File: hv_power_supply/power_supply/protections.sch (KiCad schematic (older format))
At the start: 50 parts, among them J1 CONN_01x02, K1 CPC1979J, Q2 SSM3K333R, Q3 SSM3K333R, Q4 FQD2N60CTM, U3 CPC1117NTR, U4 ACPL-C79B-500E, U5 ACPL-C87B-000E, U6 LT-1997-2, U7 ADA4661-2

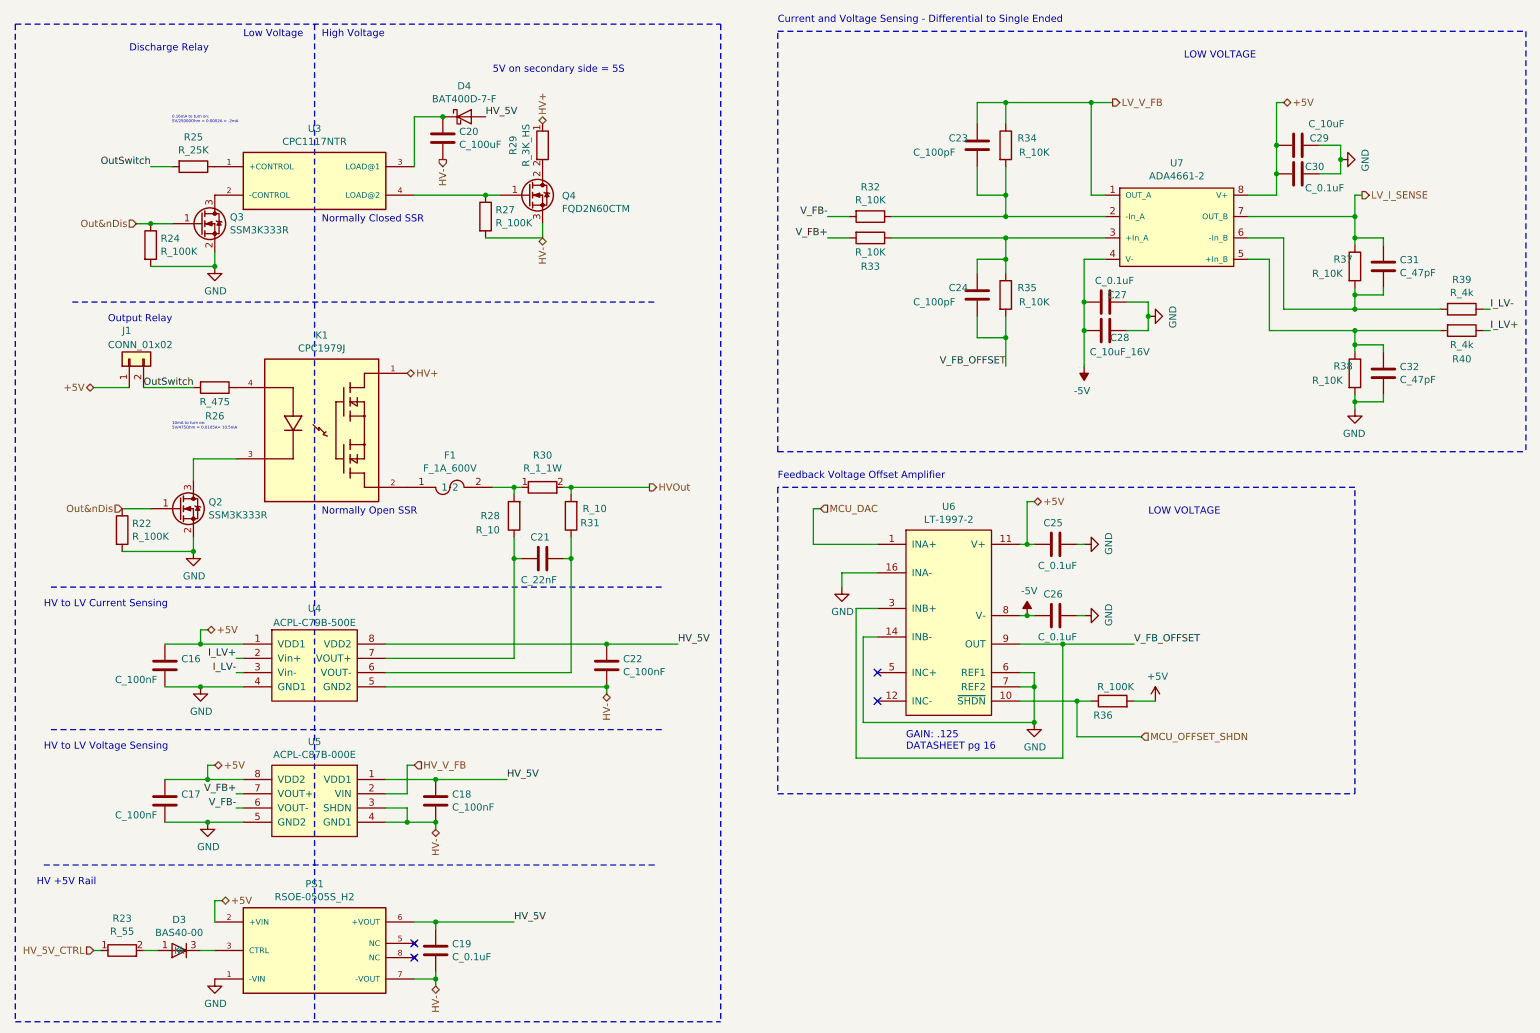
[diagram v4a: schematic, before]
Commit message: updated MCU pins
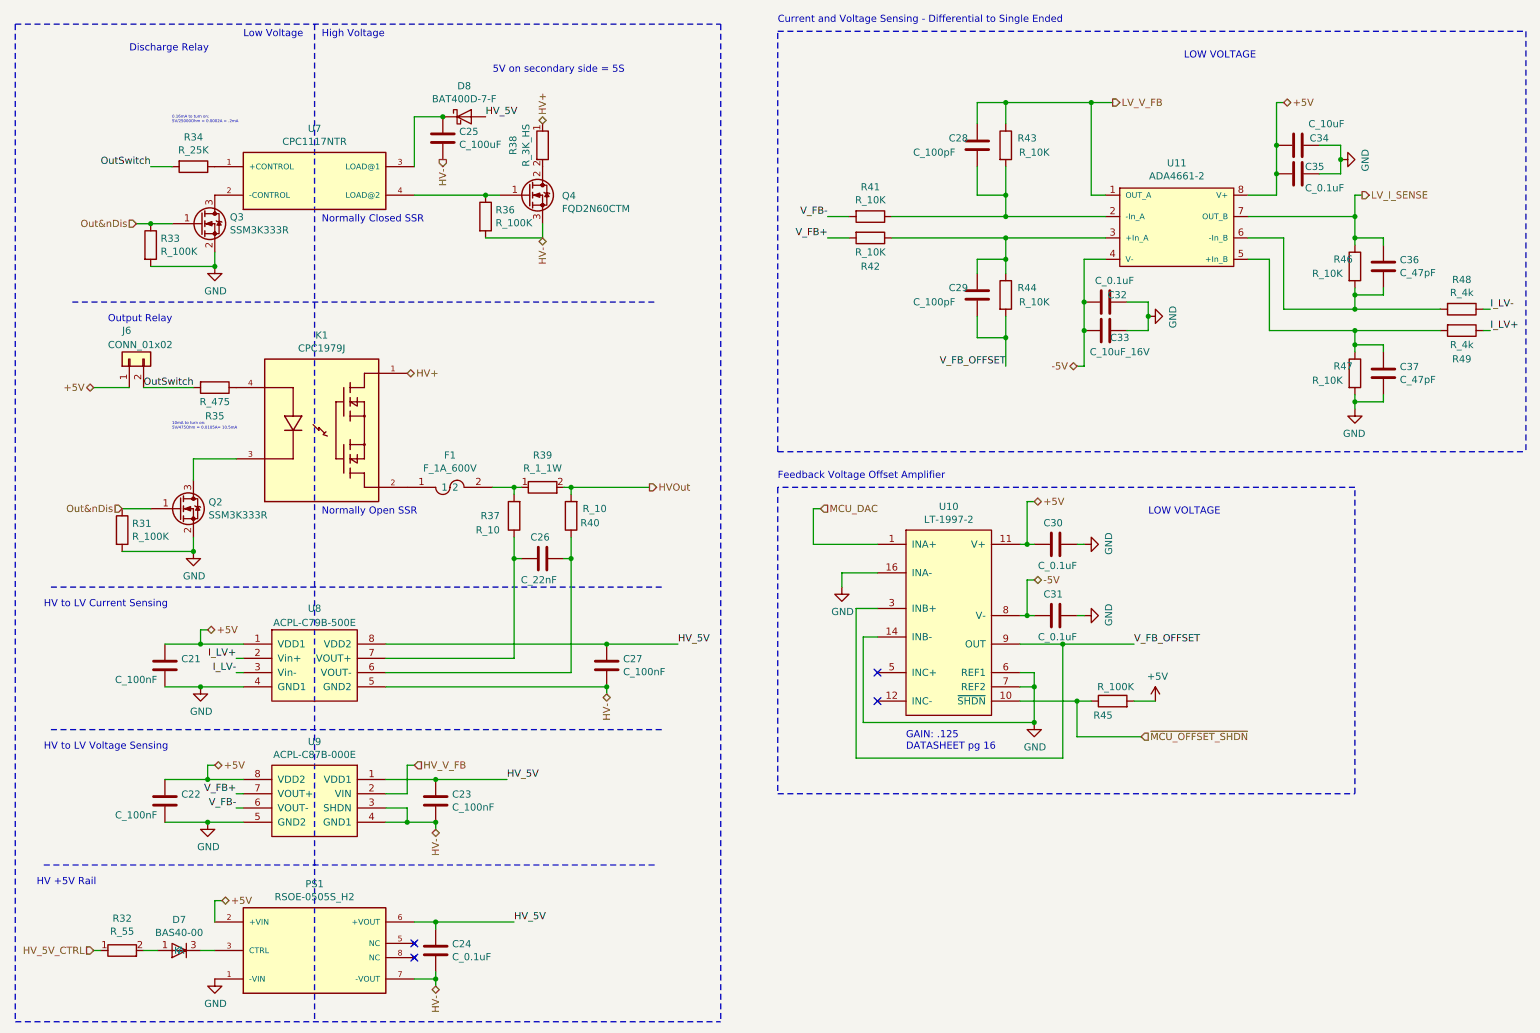
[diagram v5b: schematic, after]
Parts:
- renumbered C16 to C21, C17 to C22, C18 to C23, C19 to C24, C20 to C25, C21 to C26, C22 to C27, C23 to C28, C24 to C29, C25 to C30, C26 to C31, C27 to C32, C28 to C33, C29 to C34, C30 to C35, C31 to C36, C32 to C37, D3 to D7, D4 to D8, J1 to J6, R22 to R31, R23 to R32, R24 to R33, R25 to R34, R26 to R35, R27 to R36, R28 to R37, R29 to R38, R30 to R39, R31 to R40, R32 to R41, R33 to R42, R34 to R43, R35 to R44, R36 to R45, R37 to R46, R38 to R47, R39 to R48, R40 to R49, U6 to U10, U7 to U11, U3 to U7, U4 to U8, U5 to U9
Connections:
- net MCU_OFFSET_SHDN renamed ~MCU_OFFSET_SHDN

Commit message: Fixed all component footprint issues, beginning to lay out flyback portion
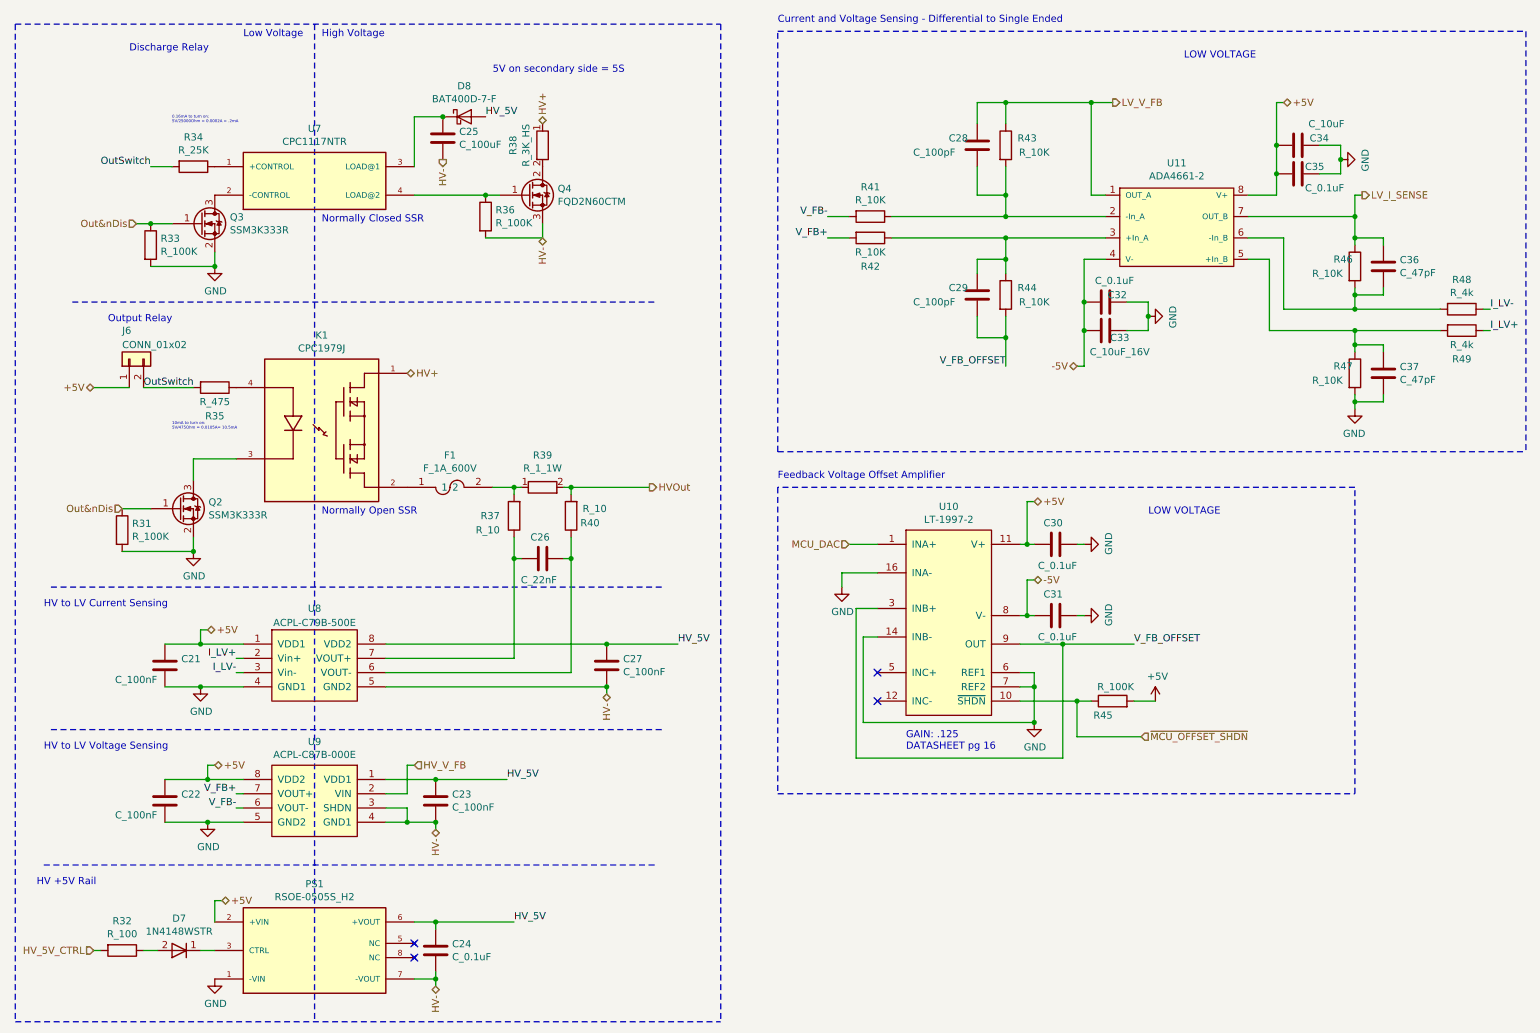
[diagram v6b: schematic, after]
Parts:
- removed D7: BAS40-00, Package_TO_SOT_SMD:SOT-23, symbol formula:BAS40-00
- removed R32: R_55, symbol formula:R_55
- added D7: 1N4148WSTR, formula:SOD-323, symbol formula:1N4148WSTR
- added R32: R_100, footprints:R_0805_OEM, symbol formula:R_100
- J6: footprint Connector_PinHeader_2.54mm:PinHeader_1x02_P2.54mm_Vertical -> footprints:PinHeader_1x02_P2.54mm_Vertical
- U7: footprint SOIC254P610X218-4N -> footprints:SOIC254P610X218-4N
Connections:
- net HV_5V_CTRL: now also R32.2
- net at PS1.3 (CTRL): now also D7.1
- new net: D7.2, R32.1
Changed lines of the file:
@@
-	1    0    0    -1
-$EndComp
-$Comp
-L formula:FQD2N60CTM Q4
-U 1 1 5FD240E6
-P 4250 2000
-F 0 "Q4" H 4386 2046 50  0000 L CNN
-F 1 "FQD2N60CTM" H 4386 1955 50  0000 L CNN
-F 2 "footprints:DPAK229P990X239-4N" H 4240 2460 50  0001 C CNN
-F 3 "https://www.onsemi.com/pub/Collateral/FQU2N60C-D.PDF" H 4250 2000 50  0001 C CNN
-F 4 "ON Semiconductor" H 4250 2000 50  0001 C CNN "MFN"
-F 5 "FDB33N25TM" H 4250 2000 50  0001 C CNN "MPN"
-F 6 "https://www.digikey.com/en/products/detail/on-semiconductor/FQD2N60CTM/1053993" H 4250 2000 50  0001 C CNN "Purchasing Link"
-	1    4250 2000
 	1    0    0    -1
 $EndComp
@@
 Wire Wire Line
 	3850 1950 3950 1950
-$Comp
-L formula:CPC1117NTR U7
-U 1 1 602537FD
-P 2650 1850
-F 0 "U7" H 2650 2217 50  0000 C CNN
-F 1 "CPC1117NTR" H 2650 2126 50  0000 C CNN
-F 2 "SOIC254P610X218-4N" H 2650 1850 50  0001 L BNN
-F 3 "https://www.ixysic.com/home/pdfs.nsf/www/CPC1117N.pdf/$file/CPC1117N.pdf" H 2650 1850 50  0001 L BNN
-F 4 "IXYS" H 2650 1850 50  0001 L BNN "MANUFACTURER"
-F 5 "https://www.digikey.com/en/products/detail/ixys-integrated-circuits-division/CPC1117NTR/1277122" H 2650 1850 50  0001 C CNN "Purchasing"
-	1    2650 1850
-	1    0    0    -1
-$EndComp
 Wire Wire Line
 	3550 1400 3350 1400
@@
 	1    0    0    -1
 $EndComp
-$Comp
-L formula:CONN_01x02 J6
-U 1 1 6035D5F6
-P 1350 3100
-F 0 "J6" V 1550 3150 50  0000 R CNN
-F 1 "CONN_01x02" V 1450 3250 50  0000 R CNN
-F 2 "Connector_PinHeader_2.54mm:PinHeader_1x02_P2.54mm_Vertical" H 1250 3100 50  0001 C CNN
-F 3 "https://katalog.we-online.de/em/datasheet/6130xx11121.pdf" H 1350 3200 50  0001 C CNN
-F 4 "DK" H 1450 3300 50  0001 C CNN "MFN"
-F 5 "732-5315-ND" H 1550 3400 50  0001 C CNN "MPN"
-	1    1350 3100
-	0    -1   -1   0
-$EndComp
 Text HLabel 1300 4150 0    50   Input ~ 0
 Out&nDis
@@
 	1    0    0    -1
 $EndComp
-Wire Wire Line
-	6150 4150 6150 4400
-Wire Wire Line
-	6150 4400 6600 4400
 $Comp
 L formula:C_0.1uF C30
@@
 	-1   0    0    1
 $EndComp
-$Comp
-L formula:BAS40-00 D7
-U 1 1 60FD2663
-P 1700 7250
-F 0 "D7" H 1700 7034 50  0000 C CNN
-F 1 "BAS40-00" H 1700 7125 50  0000 C CNN
-F 2 "Package_TO_SOT_SMD:SOT-23" H 1600 7250 50  0001 C CNN
-F 3 "https://assets.nexperia.com/documents/data-sheet/BAS40_1PSXXSB4X_SER.pdf" H 1700 7350 50  0001 C CNN
-F 4 "DK" H 1800 7450 50  0001 C CNN "MFN"
-F 5 "1727-4234-1-ND" H 1900 7550 50  0001 C CNN "MPN"
-F 6 "https://www.digikey.com/product-detail/en/nexperia-usa-inc/BAS40215/1727-4234-1-ND/2122190" H 2000 7650 50  0001 C CNN "PurchasingLink"
-	1    1700 7250
-	-1   0    0    1
-$EndComp
 Wire Wire Line
 	1850 7250 1950 7250
@@
 Wire Wire Line
 	1850 5400 2150 5400
-$Comp
-L formula:R_55 R32
-U 1 1 60FD266E
-P 1300 7250
-F 0 "R32" H 1300 7475 50  0000 C CNN
-F 1 "R_55" H 1300 7384 50  0000 C CNN
-F 2 "" V 1300 7250 50  0001 C CNN
-F 3 "" V 1300 7250 50  0001 C CNN
-	1    1300 7250
-	1    0    0    -1
-$EndComp
 Wire Wire Line
 	1450 7250 1550 7250
@@
 Wire Wire Line
 	9950 1950 10000 1950
-Text HLabel 6200 4150 2    50   Input ~ 0
+Text HLabel 6400 4400 0    50   Input ~ 0
 MCU_DAC
-Wire Wire Line
-	6150 4150 6200 4150
 Text HLabel 8450 5750 2    50   Input ~ 0
 ~MCU_OFFSET_SHDN
@@
 Wire Wire Line
 	8050 3150 8000 3150
+$Comp
+L formula:R_100 R32
+U 1 1 60632281
+P 1300 7250
+F 0 "R32" V 1093 7250 50  0000 C CNN
+F 1 "R_100" V 1184 7250 50  0000 C CNN
+F 2 "footprints:R_0805_OEM" H 500 7400 50  0001 C CNN
+F 3 "https://www.seielect.com/Catalog/SEI-rncp.pdf" H 1000 7750 50  0001 C CNN
+F 4 "DK" H 1300 7250 60  0001 C CNN "MFN"
+F 5 "RNCP0805FTD100RCT-ND" H 650 7500 60  0001 C CNN "MPN"
+F 6 "https://www.digikey.com/products/en?keywords=RNCP0805FTD100RCT-ND" H 1780 7650 60  0001 C CNN "PurchasingLink"
+	1    1300 7250
+	0    1    1    0
+$EndComp
+Wire Wire Line
+	6400 4400 6600 4400
+$Comp
+L formula:1N4148WSTR D7
+U 1 1 60678A17
+P 1700 7250
+F 0 "D7" H 1700 7475 50  0000 C CNN
+F 1 "1N4148WSTR" H 1700 7384 50  0000 C CNN
+F 2 "formula:SOD-323" H 1650 7400 50  0001 C CNN
+F 3 "http://www.smc-diodes.com/propdf/1N4148WS%20N0572%20REV.B.pdf" H 1650 7400 50  0001 C CNN
+F 4 "https://www.digikey.com/en/products/detail/smc-diode-solutions/1N4148WSTR/6022449" H 1700 7450 50  0001 C CNN "Purchasing Link"
+F 5 "SMC Diode" H 1400 7500 50  0001 C CNN "MFN"
+F 6 "1N4148WSTR" H 1700 7650 50  0001 C CNN "MPN"
+	1    1700 7250
+	1    0    0    -1
+$EndComp
+$Comp
+L formula:CPC1117NTR U7
+U 1 1 6067B7A7
+P 2650 1850
+F 0 "U7" H 2650 2217 50  0000 C CNN
+F 1 "CPC1117NTR" H 2650 2126 50  0000 C CNN
+F 2 "footprints:SOIC254P610X218-4N" H 2650 1850 50  0001 L BNN
+F 3 "https://www.ixysic.com/home/pdfs.nsf/www/CPC1117N.pdf/$file/CPC1117N.pdf" H 2650 1850 50  0001 L BNN
+F 4 "IXYS" H 2650 1850 50  0001 L BNN "MANUFACTURER"
+F 5 "https://www.digikey.com/en/products/detail/ixys-integrated-circuits-division/CPC1117NTR/1277122" H 2650 1850 50  0001 C CNN "Purchasing"
+	1    2650 1850
+	1    0    0    -1
+$EndComp
+$Comp
+L formula:FQD2N60CTM Q4
+U 1 1 6067C482
+P 4250 2000
+F 0 "Q4" H 4356 2096 50  0000 L CNN
+F 1 "FQD2N60CTM" H 4356 2005 50  0000 L CNN
+F 2 "footprints:DPAK229P990X239-4N" H 4210 2510 50  0001 C CNN
+F 3 "https://www.onsemi.com/pub/Collateral/FQU2N60C-D.PDF" H 4220 2050 50  0001 C CNN
+F 4 "ON Semiconductor" H 4220 2050 50  0001 C CNN "MFN"
+F 5 "FDB33N25TM" H 4220 2050 50  0001 C CNN "MPN"
+F 6 "https://www.digikey.com/en/products/detail/on-semiconductor/FQD2N60CTM/1053993" H 4220 2050 50  0001 C CNN "Purchasing Link"
+	1    4250 2000
+	1    0    0    -1
+$EndComp
+$Comp
+L formula:CONN_01x02 J6
+U 1 1 6063246B
+P 1350 3100
+F 0 "J6" V 1550 3150 50  0000 R CNN
+F 1 "CONN_01x02" V 1450 3150 50  0000 R CNN
+F 2 "footprints:PinHeader_1x02_P2.54mm_Vertical" H 1250 3100 50  0001 C CNN
+F 3 "https://katalog.we-online.de/em/datasheet/6130xx11121.pdf" H 1350 3200 50  0001 C CNN
+F 4 "DK" H 1450 3300 50  0001 C CNN "MFN"
+F 5 "732-5315-ND" H 1550 3400 50  0001 C CNN "MPN"
+	1    1350 3100
+	0    -1   -1   0
+$EndComp
 $EndSCHEMATC
